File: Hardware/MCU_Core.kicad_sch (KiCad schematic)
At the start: 4 parts, among them U1 STM32F407VETx

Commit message: Init SCH
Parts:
- added C1, C3, C4, C5, C6, C7, C8: 0.1uF, symbol Device:C
- added C9: 1uF, symbol Device:C
- added R3: CSTCE16M00G55-R0, CSTCE12M0G55-R0, symbol SamacSys_Parts:CSTCE8M00G55-R0
- renumbered C1 to C2
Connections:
- net +3.3V: now also C1.1, C3.1, C4.1, C5.1, C6.1, C7.1, C8.1, C9.1
- net GND: now also C1.2, C3.2, C4.2, C5.2, C6.2, C7.2, C8.2, C9.2
- net OSCH_IN: now reaches U1.12 (PH0)
- net OSCH_OUT: now reaches U1.13 (PH1)

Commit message: Finished SCH MCU
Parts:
- added C10, C11: 2.2uF, symbol Device:C
- added C12, C13: 0.1uF, symbol Device:C
- added J1: SWD_Port, symbol Connector:Conn_01x04_Socket
- added J2: Conn_01x04_Socket, symbol Connector:Conn_01x04_Socket
- added JP1: BOOT0, symbol Jumper:SolderJumper_3_Open
- added L1: 0R, symbol Device:L
- added R4: 100R, symbol Device:R
- added S1: RST, B3U-1000P, symbol SamacSys_Parts:B3U-1000P
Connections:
- net +3.3V: now also C12.1, J1.1 (Pin_1), J2.1 (Pin_1), L1.1, R4.2; no longer C8.1, C9.1, U1.22 (VDDA)
- net BOOT0: now also JP1.2 (C); no longer R2.1
- net GND: now also R3.2, C10.2, C11.2, C12.2, C13.2, J1.4 (Pin_4), J2.4 (Pin_4), S1.1 (K)
- net NRST: now also S1.2 (A)
- net OSCH_IN: now also R3.1
- net OSCH_OUT: now also R3.3
- net +3.3VADC: now reaches U1.21 (VREF+)
- net +3.3VADC: now also C8.1, C9.1, U1.22 (VDDA), C13.1, L1.2
- net VCAP_1: now reaches U1.49 (VCAP_1)
- net VCAP_1: now also C10.1
- net SWDIO: now reaches U1.72 (PA13)
- net SWDIO: now also J1.2 (Pin_2)
- net VCAP_2: now reaches U1.73 (VCAP_2)
- net VCAP_2: now also C11.1
- net SWCLK: now reaches U1.76 (PA14)
- net SWCLK: now also J1.3 (Pin_3)
- net Dbg_TX: now reaches U1.80 (PC12)
- net Dbg_TX: now also J2.3 (Pin_3)
- net Dbg_RX: now reaches U1.83 (PD2)
- net Dbg_RX: now also J2.2 (Pin_2)
- new net: JP1.1 (A), R4.1
- new net: JP1.3 (B), R2.1
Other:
- moved on the sheet: C1, C2, C3, C4, C5, C6, C7, R1, R3

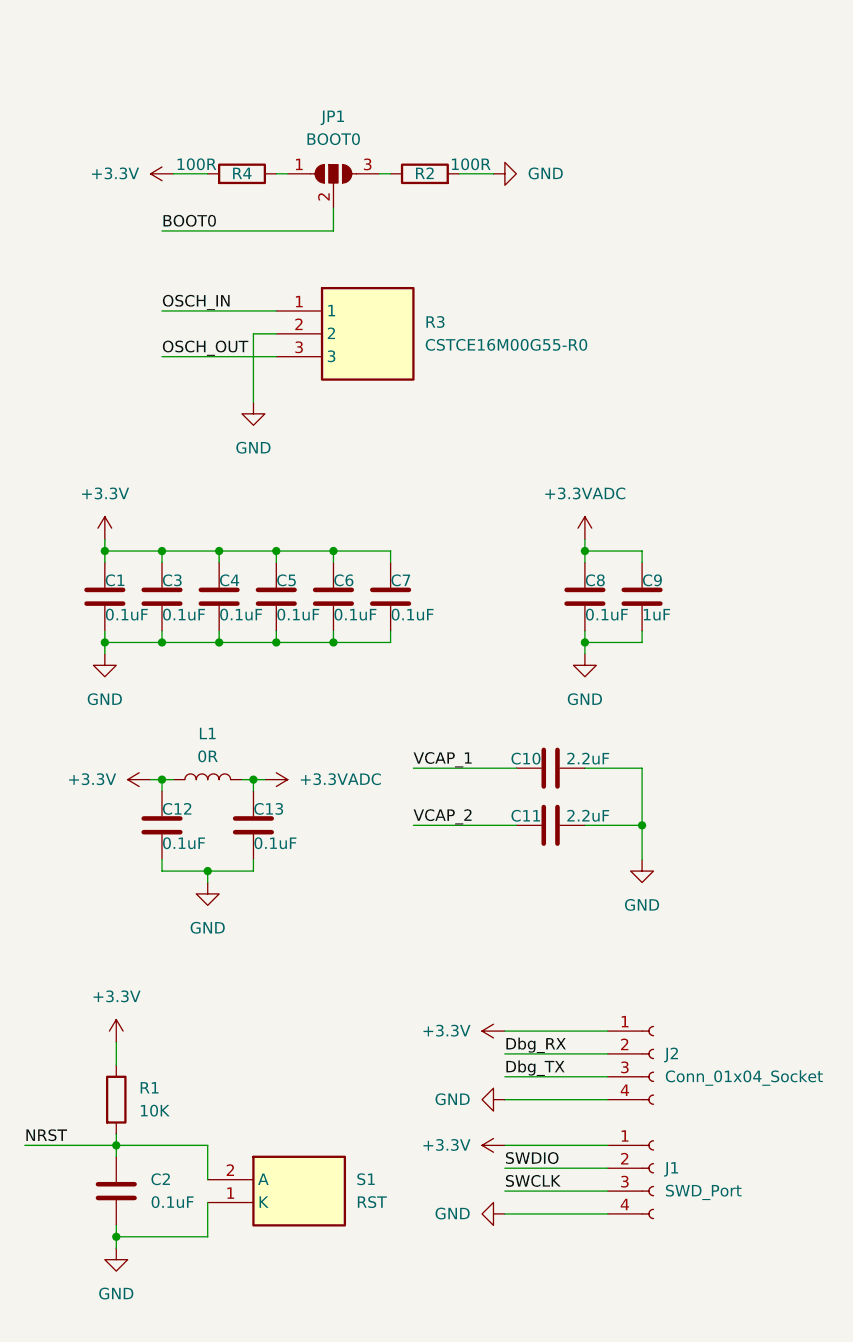
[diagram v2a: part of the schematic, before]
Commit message: Add Image Transmission
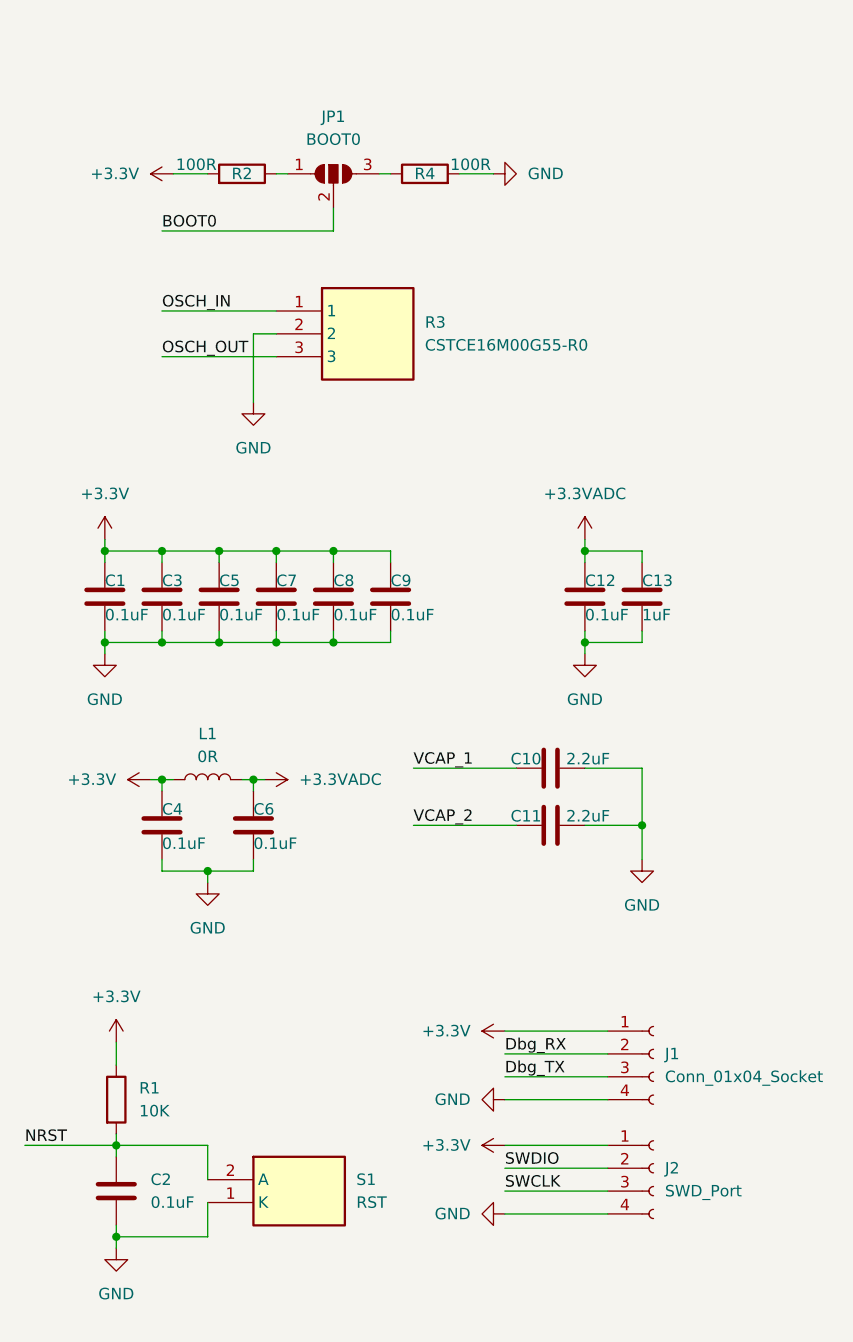
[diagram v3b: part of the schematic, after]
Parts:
- JP1: footprint (none) -> Jumper:SolderJumper-3_P1.3mm_Open_RoundedPad1.0x1.5mm
- renumbered C8 to C12, C9 to C13, C12 to C4, C4 to C5, C13 to C6, C5 to C7, C6 to C8, C7 to C9, J2 to J1, J1 to J2, R4 to R2, R2 to R4
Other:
- company: (none) -> Bowen_Meng

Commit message: Update PCB
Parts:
- C1, C10, C11, C12, C13, C2, C3, C4, C5, C6, C7, C8, C9: footprint (none) -> Capacitor_SMD:C_0603_1608Metric; symbol Device:C -> Library:C
- J1, J2: symbol Connector:Conn_01x04_Socket -> Library:Conn_01x04_Socket
- JP1: symbol Jumper:SolderJumper_3_Open -> Library:SolderJumper_3_Open
- L1: footprint (none) -> Inductor_SMD:L_0805_2012Metric; symbol Device:L -> Library:L
- R1, R2, R4: footprint (none) -> Resistor_SMD:R_0603_1608Metric; symbol Device:R -> Library:R
- R3: symbol SamacSys_Parts:CSTCE8M00G55-R0 -> Library:CSTCE8M00G55-R0
- S1: symbol SamacSys_Parts:B3U-1000P -> Library:B3U-1000P
- U1: symbol MCU_ST_STM32F4:STM32F407VETx -> Library:STM32F407VETx
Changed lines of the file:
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@@
 	)
 	(symbol
-		(lib_id "Device:C")
+		(lib_id "Library:C")
 		(at 123.19 114.3 0)
 		(unit 1)
@@
 			)
 		)
-		(property "Footprint" ""
+		(property "Footprint" "Capacitor_SMD:C_0603_1608Metric"
 			(at 124.1552 118.11 0)
 			(effects
@@
 	)
 	(symbol
-		(lib_id "Device:C")
+		(lib_id "Library:C")
 		(at 148.59 88.9 0)
 		(unit 1)
@@
 			)
 		)
-		(property "Footprint" ""
+		(property "Footprint" "Capacitor_SMD:C_0603_1608Metric"
 			(at 149.5552 92.71 0)
 			(effects
@@
 	)
 	(symbol
-		(lib_id "power:+3.3VADC")
+		(lib_id "Library:+3.3VADC")
 		(at 71.12 26.67 0)
 		(unit 1)
@@
 	)
 	(symbol
-		(lib_id "power:+3.3V")
+		(lib_id "Library:+3.3V")
 		(at 53.34 26.67 0)
 		(unit 1)
@@
 	)
 	(symbol
-		(lib_id "Device:R")
+		(lib_id "Library:R")
 		(at 132.08 41.91 270)
 		(mirror x)
@@
 			)
 		)
-		(property "Footprint" ""
+		(property "Footprint" "Resistor_SMD:R_0603_1608Metric"
 			(at 132.08 43.688 90)
 			(effects
@@
 	)
 	(symbol
-		(lib_id "Device:C")
+		(lib_id "Library:C")
 		(at 142.24 88.9 0)
 		(unit 1)
@@
 			)
 		)
-		(property "Footprint" ""
+		(property "Footprint" "Capacitor_SMD:C_0603_1608Metric"
 			(at 143.2052 92.71 0)
 			(effects
@@
 	)
 	(symbol
-		(lib_id "power:GND")
+		(lib_id "Library:GND")
 		(at 161.29 157.48 270)
 		(unit 1)
@@
 	)
 	(symbol
-		(lib_id "power:+3.3V")
+		(lib_id "Library:+3.3V")
 		(at 161.29 149.86 90)
 		(unit 1)
@@
 	)
 	(symbol
-		(lib_id "power:GND")
+		(lib_id "Library:GND")
 		(at 176.53 118.11 0)
 		(unit 1)
@@
 	)
 	(symbol
-		(lib_id "Device:R")
+		(lib_id "Library:R")
 		(at 152.4 41.91 90)
 		(unit 1)
@@
 			)
 		)
-		(property "Footprint" ""
+		(property "Footprint" "Resistor_SMD:R_0603_1608Metric"
 			(at 152.4 43.688 90)
 			(effects
@@
 	)
 	(symbol
-		(lib_id "Device:C")
+		(lib_id "Library:C")
 		(at 176.53 88.9 0)
 		(unit 1)
@@
 			)
 		)
-		(property "Footprint" ""
+		(property "Footprint" "Capacitor_SMD:C_0603_1608Metric"
 			(at 177.4952 92.71 0)
 			(effects
@@
 	)
 	(symbol
-		(lib_id "Device:C")
+		(lib_id "Library:C")
 		(at 135.89 88.9 0)
 		(unit 1)
@@
 			)
 		)
-		(property "Footprint" ""
+		(property "Footprint" "Capacitor_SMD:C_0603_1608Metric"
 			(at 136.8552 92.71 0)
 			(effects
@@
 	)
 	(symbol
-		(lib_id "Connector:Conn_01x04_Socket")
+		(lib_id "Library:Conn_01x04_Socket")
 		(at 177.8 152.4 0)
 		(unit 1)
@@
 	)
 	(symbol
-		(lib_id "Device:C")
+		(lib_id "Library:C")
 		(at 123.19 88.9 0)
 		(unit 1)
@@
 			)
 		)
-		(property "Footprint" ""
+		(property "Footprint" "Capacitor_SMD:C_0603_1608Metric"
 			(at 124.1552 92.71 0)
 			(effects
@@
 	)
 	(symbol
-		(lib_id "power:GND")
+		(lib_id "Library:GND")
 		(at 160.02 41.91 90)
 		(unit 1)
@@
 	)
 	(symbol
-		(lib_id "Device:C")
+		(lib_id "Library:C")
 		(at 133.35 114.3 0)
 		(unit 1)
@@
 			)
 		)
-		(property "Footprint" ""
+		(property "Footprint" "Capacitor_SMD:C_0603_1608Metric"
 			(at 134.3152 118.11 0)
 			(effects
@@
 	)
 	(symbol
-		(lib_id "Device:C")
+		(lib_id "Library:C")
 		(at 116.84 88.9 0)
 		(unit 1)
@@
 			)
 		)
-		(property "Footprint" ""
+		(property "Footprint" "Capacitor_SMD:C_0603_1608Metric"
 			(at 117.8052 92.71 0)
 			(effects
@@
 	)
 	(symbol
-		(lib_id "Device:C")
+		(lib_id "Library:C")
 		(at 170.18 88.9 0)
 		(unit 1)
@@
 			)
 		)
-		(property "Footprint" ""
+		(property "Footprint" "Capacitor_SMD:C_0603_1608Metric"
 			(at 171.1452 92.71 0)
 			(effects
@@
 	)
 	(symbol
-		(lib_id "power:GND")
+		(lib_id "Library:GND")
 		(at 161.29 144.78 270)
 		(unit 1)
@@
 	)
 	(symbol
-		(lib_id "Device:C")
+		(lib_id "Library:C")
 		(at 166.37 107.95 90)
 		(unit 1)
@@
 			)
 		)
-		(property "Footprint" ""
+		(property "Footprint" "Capacitor_SMD:C_0603_1608Metric"
 			(at 170.18 106.9848 0)
 			(effects
@@
 	)
 	(symbol
-		(lib_id "power:+3.3V")
+		(lib_id "Library:+3.3V")
 		(at 124.46 41.91 90)
 		(unit 1)
@@
 	)
 	(symbol
-		(lib_id "power:+3.3V")
+		(lib_id "Library:+3.3V")
 		(at 118.11 138.43 0)
 		(unit 1)
@@
 	)
 	(symbol
-		(lib_id "power:GND")
+		(lib_id "Library:GND")
 		(at 116.84 95.25 0)
 		(unit 1)
@@
 	)
 	(symbol
-		(lib_id "Connector:Conn_01x04_Socket")
+		(lib_id "Library:Conn_01x04_Socket")
 		(at 177.8 139.7 0)
 		(unit 1)
@@
 	)
 	(symbol
-		(lib_id "power:GND")
+		(lib_id "Library:GND")
 		(at 133.35 67.31 0)
 		(unit 1)
@@
 	)
 	(symbol
-		(lib_id "SamacSys_Parts:CSTCE8M00G55-R0")
+		(lib_id "Library:CSTCE8M00G55-R0")
 		(at 135.89 57.15 0)
 		(unit 1)
@@
 	)
 	(symbol
-		(lib_id "power:+3.3VADC")
+		(lib_id "Library:+3.3VADC")
 		(at 134.62 109.22 270)
 		(unit 1)
@@
 	)
 	(symbol
-		(lib_id "SamacSys_Parts:B3U-1000P")
+		(lib_id "Library:B3U-1000P")
 		(at 128.27 153.67 0)
 		(unit 1)
@@
 	)
 	(symbol
-		(lib_id "power:GND")
+		(lib_id "Library:GND")
 		(at 118.11 161.29 0)
 		(unit 1)
@@
 	)
 	(symbol
-		(lib_id "Device:L")
+		(lib_id "Library:L")
 		(at 128.27 109.22 90)
 		(unit 1)
@@
 			)
 		)
-		(property "Footprint" ""
+		(property "Footprint" "Inductor_SMD:L_0805_2012Metric"
 			(at 128.27 109.22 0)
 			(effects
@@
 	)
 	(symbol
-		(lib_id "Device:C")
+		(lib_id "Library:C")
 		(at 118.11 154.94 0)
 		(unit 1)
@@
 			)
 		)
-		(property "Footprint" ""
+		(property "Footprint" "Capacitor_SMD:C_0603_1608Metric"
 			(at 119.0752 158.75 0)
 			(effects
@@
 	)
 	(symbol
-		(lib_id "MCU_ST_STM32F4:STM32F407VETx")
+		(lib_id "Library:STM32F407VETx")
 		(at 60.96 102.87 0)
 		(unit 1)
@@
 	)
 	(symbol
-		(lib_id "power:+3.3V")
+		(lib_id "Library:+3.3V")
 		(at 116.84 82.55 0)
 		(unit 1)
@@
 	)
 	(symbol
-		(lib_id "power:GND")
+		(lib_id "Library:GND")
 		(at 170.18 95.25 0)
 		(unit 1)
@@
 	)
 	(symbol
-		(lib_id "power:+3.3V")
+		(lib_id "Library:+3.3V")
 		(at 161.29 137.16 90)
 		(unit 1)
@@
 	)
 	(symbol
-		(lib_id "power:GND")
+		(lib_id "Library:GND")
 		(at 60.96 179.07 0)
 		(unit 1)
@@
 	)
 	(symbol
-		(lib_id "Device:C")
+		(lib_id "Library:C")
 		(at 129.54 88.9 0)
 		(unit 1)
@@
 			)
 		)
-		(property "Footprint" ""
+		(property "Footprint" "Capacitor_SMD:C_0603_1608Metric"
 			(at 130.5052 92.71 0)
 			(effects
@@
 	)
 	(symbol
-		(lib_id "power:+3.3V")
+		(lib_id "Library:+3.3V")
 		(at 121.92 109.22 90)
 		(unit 1)
@@
 	)
 	(symbol
-		(lib_id "Device:R")
+		(lib_id "Library:R")
 		(at 118.11 144.78 0)
 		(unit 1)
@@
 			)
 		)
-		(property "Footprint" ""
+		(property "Footprint" "Resistor_SMD:R_0603_1608Metric"
 			(at 116.332 144.78 90)
 			(effects
@@
 	)
 	(symbol
-		(lib_id "power:+3.3VADC")
+		(lib_id "Library:+3.3VADC")
 		(at 26.67 49.53 90)
 		(unit 1)
@@
 	)
 	(symbol
-		(lib_id "Jumper:SolderJumper_3_Open")
+		(lib_id "Library:SolderJumper_3_Open")
 		(at 142.24 41.91 0)
 		(unit 1)
@@
 	)
 	(symbol
-		(lib_id "power:+3.3VADC")
+		(lib_id "Library:+3.3VADC")
 		(at 170.18 82.55 0)
 		(unit 1)
@@
 	)
 	(symbol
-		(lib_id "Device:C")
+		(lib_id "Library:C")
 		(at 166.37 114.3 90)
 		(unit 1)
@@
 			)
 		)
-		(property "Footprint" ""
+		(property "Footprint" "Capacitor_SMD:C_0603_1608Metric"
 			(at 170.18 113.3348 0)
 			(effects
@@
 	)
 	(symbol
-		(lib_id "power:GND")
+		(lib_id "Library:GND")
 		(at 128.27 120.65 0)
 		(unit 1)
